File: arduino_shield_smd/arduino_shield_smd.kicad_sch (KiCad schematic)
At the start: 44 parts, among them J1 Power, J2 Digital/PWM, J3 Analog, J4 Digital/PWM, J5 1X5 2.5mm, J6 1x2 2.5mm, U1 PCF8574T, U2 ULN2803A, U3 PCF8574T, U4 ULN2803A

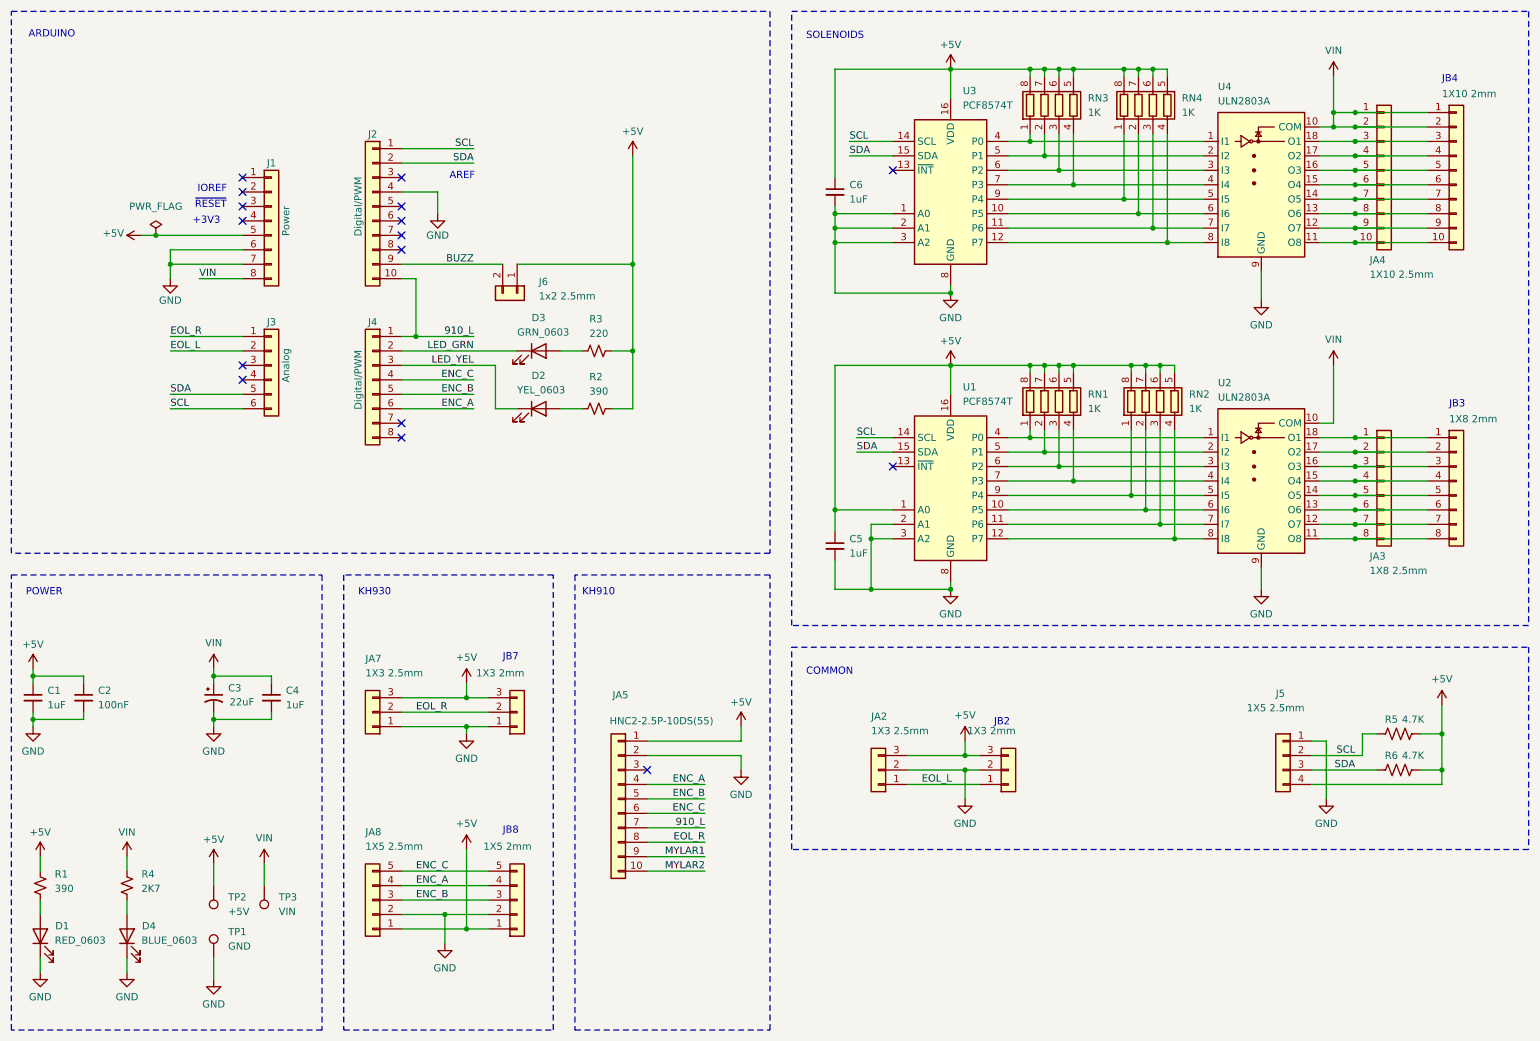
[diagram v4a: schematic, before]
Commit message: Fix ERC errors
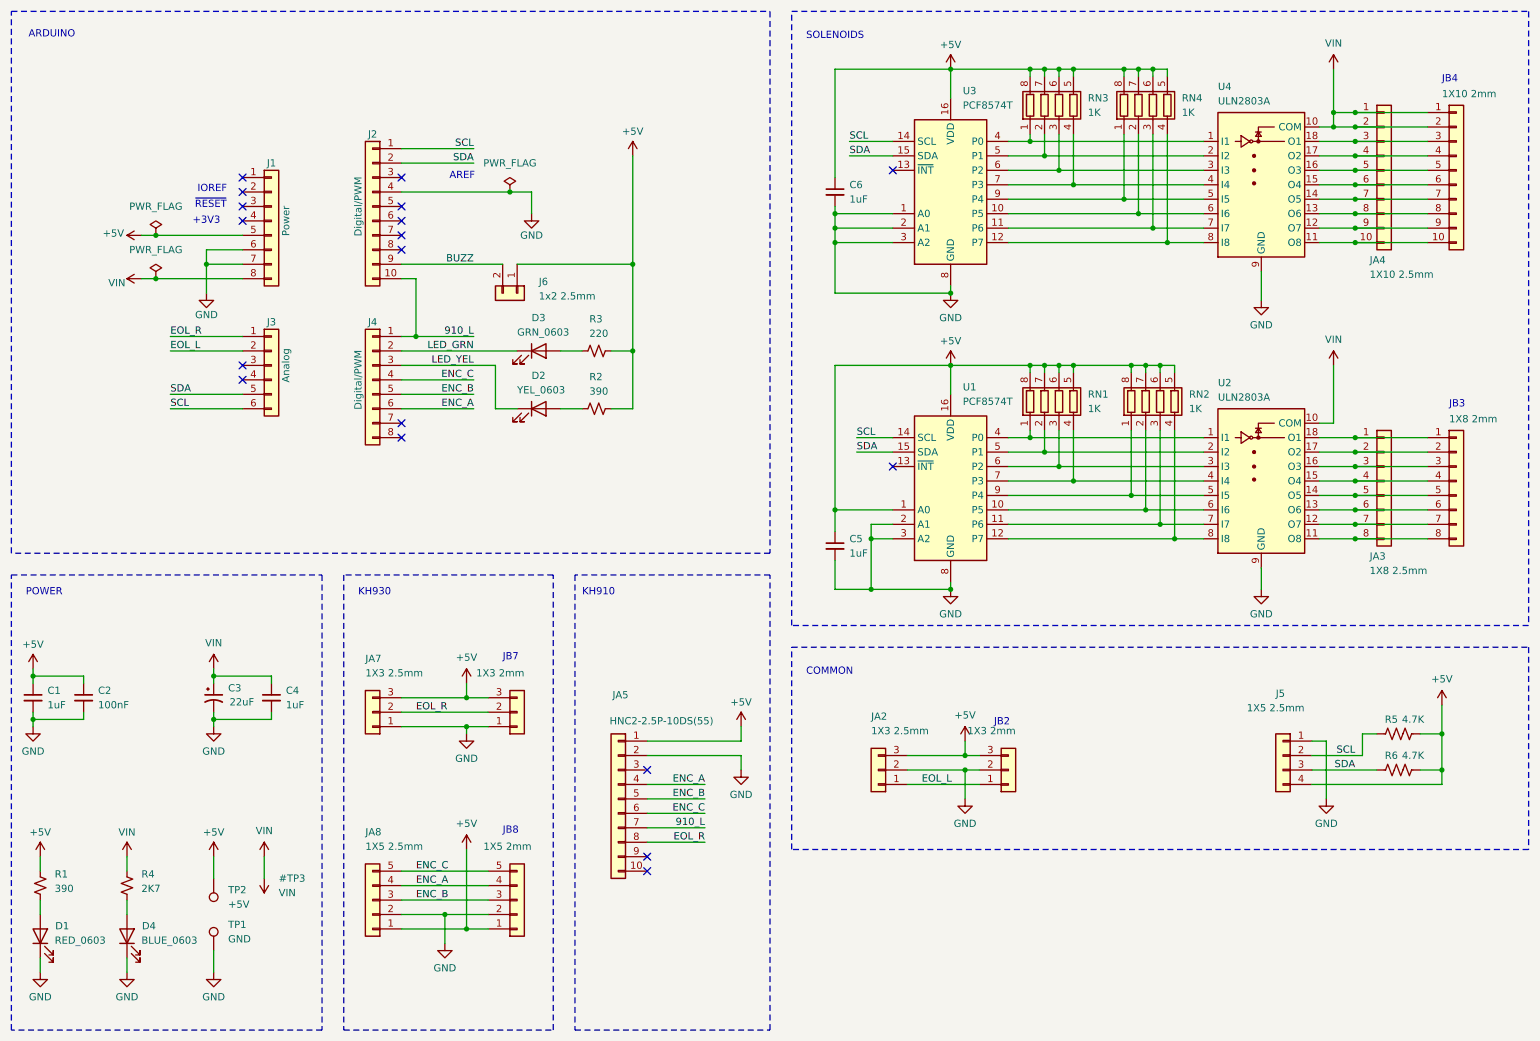
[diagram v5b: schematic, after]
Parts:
- removed TP3: VIN, TestPoint:TestPoint_THTPad_3.0x3.0mm_Drill1.5mm, symbol Connector:TestPoint
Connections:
- net MYLAR1: no longer names the net of JA5.9 (Pin_9)
- net MYLAR2: no longer names the net of JA5.10 (Pin_10)
- no-connect marks 16 -> 18
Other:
- moved on the sheet: TP1, TP2

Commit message: Rename knitting machine connectors and fix schematic for EOL connectors
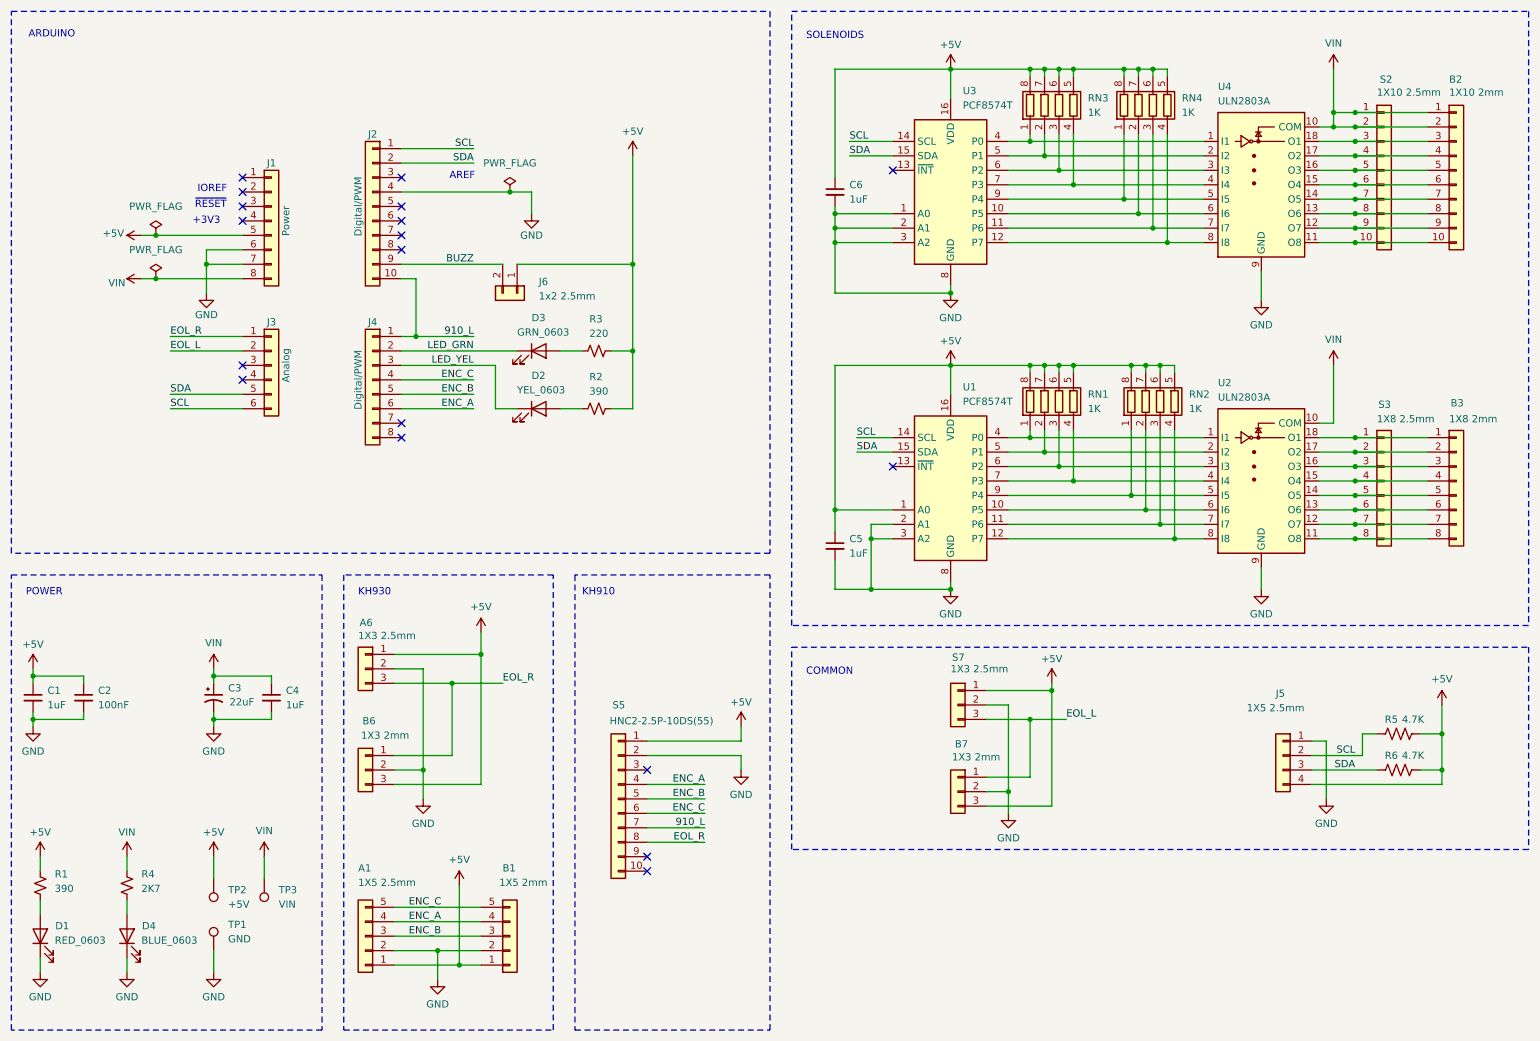
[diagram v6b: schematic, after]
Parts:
- added TP3: VIN, TestPoint:TestPoint_THTPad_3.0x3.0mm_Drill1.5mm, symbol Connector:TestPoint
- renumbered JA8 to A1, JA7 to A6, JB8 to B1, JB4 to B2, JB3 to B3, JB7 to B6, JB2 to B7, JA4 to S2, JA3 to S3, JA5 to S5, JA2 to S7
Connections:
- net +5V: now also A6.1 (Pin_1), S7.1 (Pin_1); no longer A6.3 (Pin_3), S7.3 (Pin_3)
- net EOL_L: now also S7.3 (Pin_3); no longer S7.1 (Pin_1)
- net EOL_R: now also A6.3 (Pin_3), B6.1 (Pin_1); no longer A6.2 (Pin_2), B6.2 (Pin_2)
- net GND: now also A6.2 (Pin_2), B6.2 (Pin_2); no longer A6.1 (Pin_1), B6.1 (Pin_1)
- net VIN: now also TP3.1
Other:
- note removed: "JB2"
- note removed: "JB3"
- note removed: "JB4"
- note removed: "JB7"
- note removed: "JB8"
- moved on the sheet: A1, A6, S7

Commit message: Connect S5.9 and S5.10 to GND
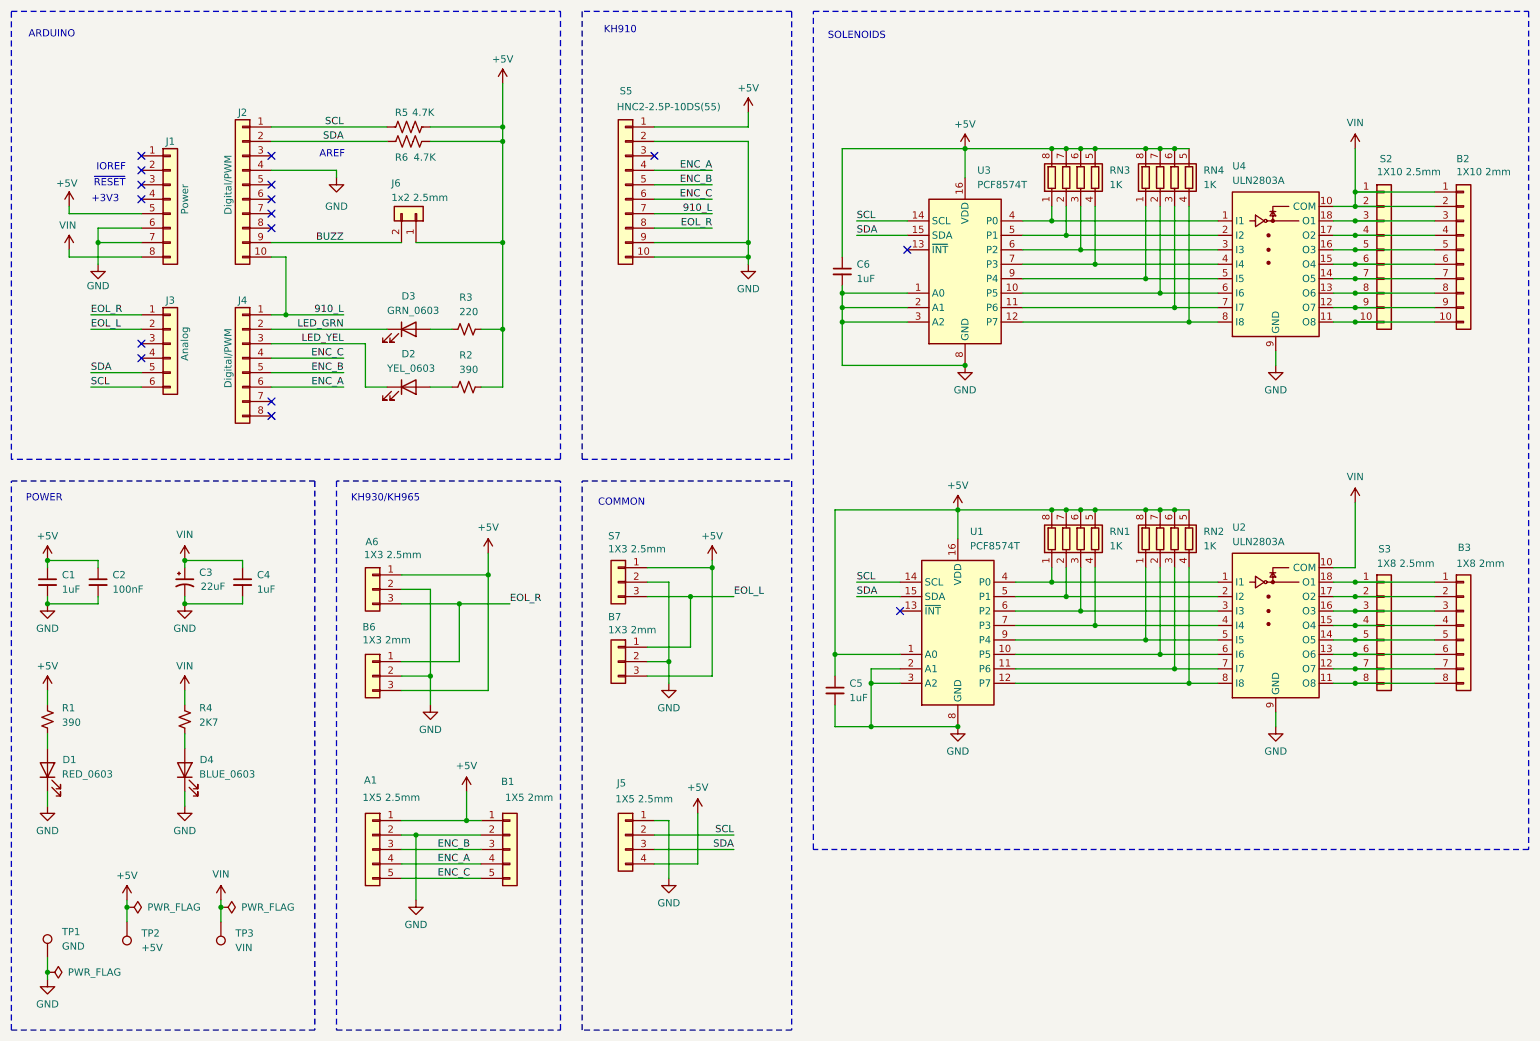
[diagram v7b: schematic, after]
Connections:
- net GND: now also S5.10 (Pin_10), S5.9 (Pin_9)
- no-connect marks 18 -> 16
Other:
- note added: "KH930/KH965"
- note removed: "KH930"
- moved on the sheet: A1, A6, B1, B2, B3, B6, B7, C1, C2, C3, C4, C5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

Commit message: Fix 2mm pitch 5-pin connector pinout
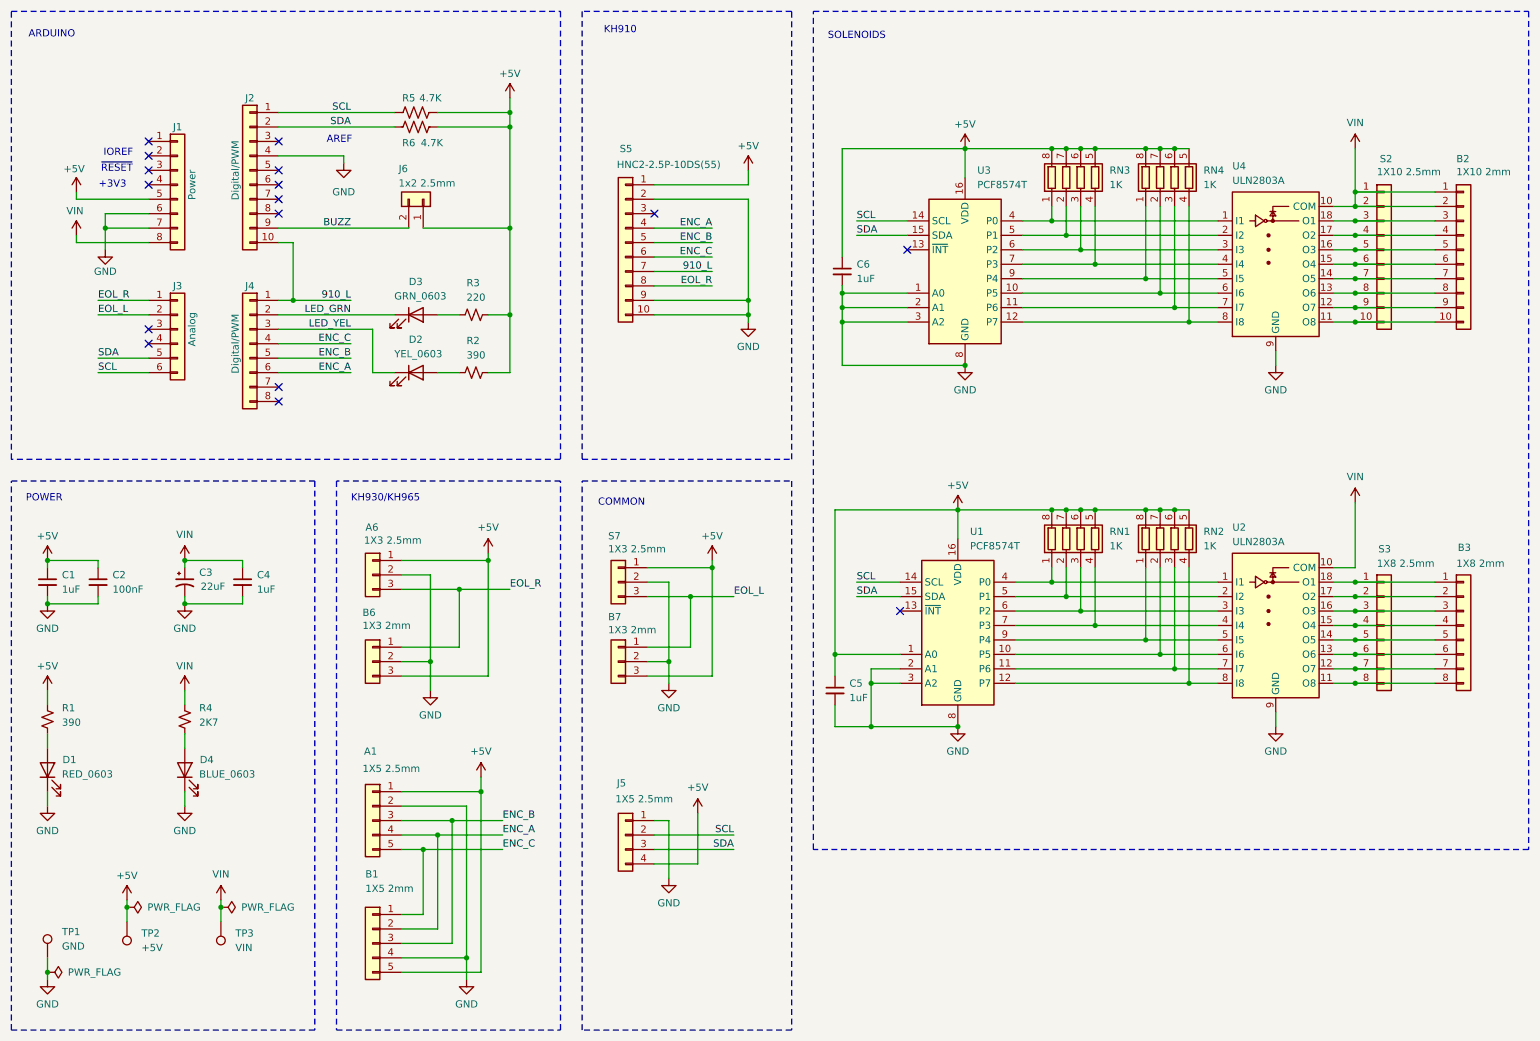
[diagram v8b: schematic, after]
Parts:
- D1, D2, D3, D4: footprint LED_SMD:LED_0805_2012Metric -> ayab-library:LED_0603_3mm_THpads
- R1, R2, R3, R4: footprint Resistor_SMD:R_0805_2012Metric -> ayab-library:R_0603_1608Metric; LCSC ID (none) -> C22790; OEM (none) -> UNI-ROYAL(Uniroyal Elec); OEM PN (none) -> 0603WAF1202T5E; Package (none) -> 0603
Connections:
- net +5V: now also B1.5 (Pin_5); no longer B1.1 (Pin_1)
- net ENC_A: now also B1.2 (Pin_2); no longer B1.4 (Pin_4)
- net ENC_C: now also B1.1 (Pin_1); no longer B1.5 (Pin_5)
- net GND: now also B1.4 (Pin_4); no longer B1.2 (Pin_2)
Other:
- moved on the sheet: A1, A6, B1, B6, D2, D3, J1, J2, J3, J4, J6, R2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
